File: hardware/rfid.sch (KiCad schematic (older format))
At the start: 1 part

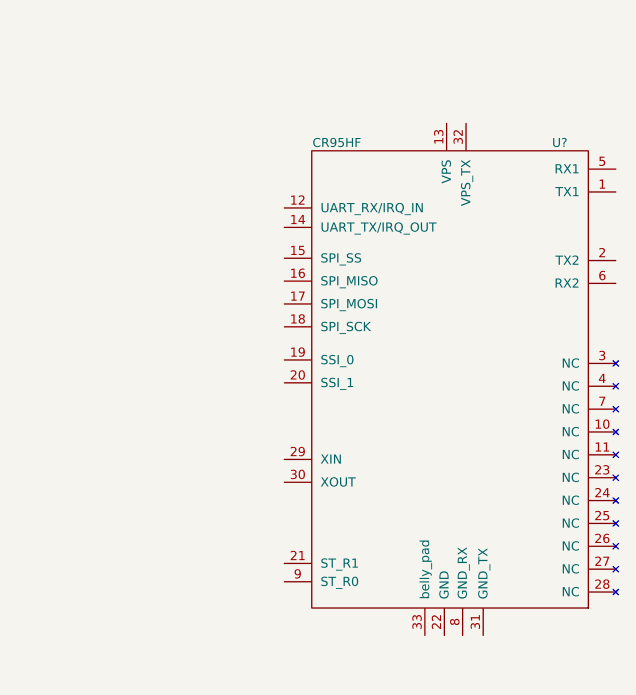
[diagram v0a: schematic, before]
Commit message: Added crystal and started connecting power to chip and extra pins.
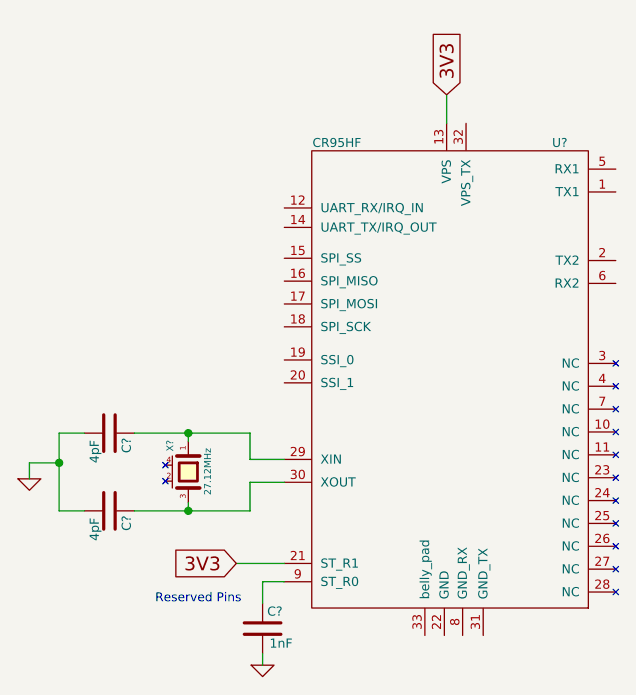
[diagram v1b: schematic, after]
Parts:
- added C? (x2): 4pF, symbol capacitor
- added C?: 1nF, symbol capacitor
- added X?: 27.12MHz, symbol MURATA_CRYSTAL_SMD
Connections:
- net 3V3: now reaches U?.13 (VPS)
- net 3V3: now also U?.21 (ST_R1)
- net at U?.29 (XIN): now also C?.1, X?.1
- net at U?.30 (XOUT): now also C?.1, X?.3
- net at U?.9 (ST_R0): now also C?.1
- new net GND: C?.2, C?.2, C?.2
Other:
- note added: "Reserved Pins"
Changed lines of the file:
@@
 	1    0    0    -1
 $EndComp
+$Comp
+L MURATA_CRYSTAL_SMD X?
+U 1 1 54173929
+P 2365 2700
+F 0 "X?" H 2250 2620 30  0000 C CNN
+F 1 "27.12MHz" H 2260 2785 30  0000 L CNN
+F 2 "" H 2365 2700 60  0000 C CNN
+F 3 "" H 2365 2700 60  0000 C CNN
+	1    2365 2700
+	0    1    1    0
+$EndComp
+$Comp
+L capacitor C?
+U 1 1 54173C81
+P 2020 2530
+F 0 "C?" H 2040 2605 40  0000 L CNN
+F 1 "4pF" H 2050 2465 40  0000 L CNN
+F 2 "" H 2058 2380 30  0000 C CNN
+F 3 "" H 2020 2530 60  0000 C CNN
+	1    2020 2530
+	0    1    1    0
+$EndComp
+$Comp
+L capacitor C?
+U 1 1 54173DFA
+P 2020 2870
+F 0 "C?" H 2040 2945 40  0000 L CNN
+F 1 "4pF" H 2050 2805 40  0000 L CNN
+F 2 "" H 2058 2720 30  0000 C CNN
+F 3 "" H 2020 2870 60  0000 C CNN
+	1    2020 2870
+	0    1    1    0
+$EndComp
+Wire Wire Line
+	2130 2530 2635 2530
+Wire Wire Line
+	2365 2530 2365 2565
+Wire Wire Line
+	2635 2530 2635 2645
+Wire Wire Line
+	2635 2645 2785 2645
+Connection ~ 2365 2530
+Wire Wire Line
+	2130 2870 2635 2870
+Wire Wire Line
+	2365 2870 2365 2835
+Wire Wire Line
+	2635 2870 2635 2745
+Wire Wire Line
+	2635 2745 2785 2745
+Connection ~ 2365 2870
+$Comp
+L GND #PWR?
+U 1 1 54173FD6
+P 1670 2730
+F 0 "#PWR?" H 1670 2730 30  0001 C CNN
+F 1 "GND" H 1670 2660 30  0001 C CNN
+F 2 "" H 1670 2730 60  0000 C CNN
+F 3 "" H 1670 2730 60  0000 C CNN
+	1    1670 2730
+	1    0    0    -1
+$EndComp
+Wire Wire Line
+	1910 2530 1800 2530
+Wire Wire Line
+	1800 2530 1800 2870
+Wire Wire Line
+	1800 2870 1910 2870
+Wire Wire Line
+	1800 2660 1670 2660
+Wire Wire Line
+	1670 2660 1670 2730
+Connection ~ 1800 2660
+$Comp
+L capacitor C?
+U 1 1 54175E86
+P 2690 3385
+F 0 "C?" H 2710 3460 40  0000 L CNN
+F 1 "1nF" H 2720 3320 40  0000 L CNN
+F 2 "" H 2728 3235 30  0000 C CNN
+F 3 "" H 2690 3385 60  0000 C CNN
+	1    2690 3385
+	1    0    0    -1
+$EndComp
+Wire Wire Line
+	2785 3180 2690 3180
+Wire Wire Line
+	2690 3180 2690 3275
+$Comp
+L GND #PWR?
+U 1 1 54175FA9
+P 2690 3545
+F 0 "#PWR?" H 2690 3545 30  0001 C CNN
+F 1 "GND" H 2690 3475 30  0001 C CNN
+F 2 "" H 2690 3545 60  0000 C CNN
+F 3 "" H 2690 3545 60  0000 C CNN
+	1    2690 3545
+	1    0    0    -1
+$EndComp
+Wire Wire Line
+	2690 3495 2690 3545
+Text Notes 2220 3280 0    39   ~ 0
+Reserved Pins
+Text GLabel 3495 1050 1    60   Input ~ 0
+3V3
+Wire Wire Line
+	3495 1175 3495 1050
+Text GLabel 2575 3100 0    60   Input ~ 0
+3V3
+Wire Wire Line
+	2785 3100 2575 3100
 $EndSCHEMATC

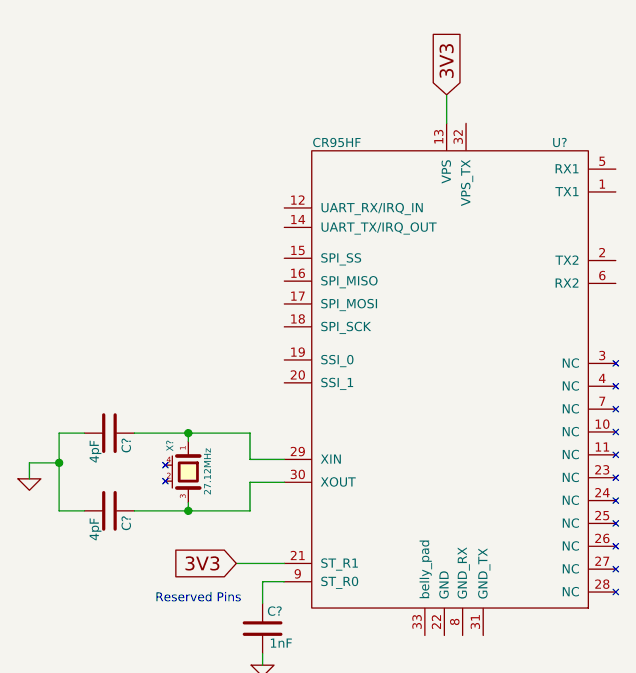
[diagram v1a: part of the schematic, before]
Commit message: Finished doing suggested pull ups, grounding, etc of certain pins. Added six pin connector for comms to micro. Not yet connected.
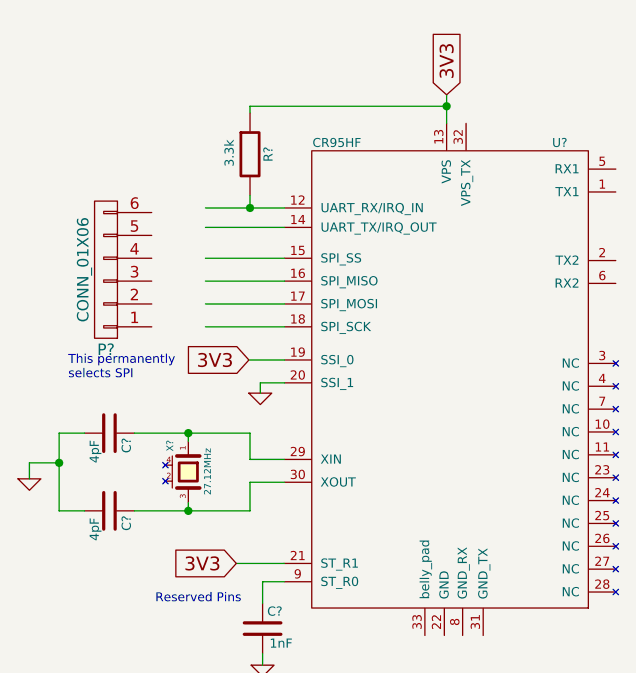
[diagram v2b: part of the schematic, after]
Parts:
- added P?: CONN_01X06, symbol CONN_01X06
- added R?: 3.3k, symbol resistor
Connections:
- wire segments 18 -> 35
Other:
- note added: "This permanently \nselects SPI"
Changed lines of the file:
@@
 $EndComp
 Wire Wire Line
-	2130 2530 2635 2530
+	2130 2530 2365 2530
+Wire Wire Line
+	2365 2530 2635 2530
 Wire Wire Line
 	2365 2530 2365 2565
@@
 Connection ~ 2365 2530
 Wire Wire Line
-	2130 2870 2635 2870
+	2130 2870 2365 2870
+Wire Wire Line
+	2365 2870 2635 2870
 Wire Wire Line
 	2365 2870 2365 2835
@@
 	1910 2530 1800 2530
 Wire Wire Line
-	1800 2530 1800 2870
+	1800 2530 1800 2660
+Wire Wire Line
+	1800 2660 1800 2870
 Wire Wire Line
 	1800 2870 1910 2870
@@
 3V3
 Wire Wire Line
-	3495 1175 3495 1050
+	3495 1175 3495 1100
+Wire Wire Line
+	3495 1100 3495 1050
 Text GLabel 2575 3100 0    60   Input ~ 0
 3V3
 Wire Wire Line
 	2785 3100 2575 3100
+$Comp
+L resistor R?
+U 1 1 54191892
+P 2635 1310
+F 0 "R?" V 2715 1310 40  0000 C CNN
+F 1 "3.3k" V 2545 1315 40  0000 C CNN
+F 2 "" V 2565 1310 30  0000 C CNN
+F 3 "" H 2635 1310 30  0000 C CNN
+	1    2635 1310
+	1    0    0    -1
+$EndComp
+Wire Wire Line
+	2440 1545 2635 1545
+Wire Wire Line
+	2635 1545 2785 1545
+Wire Wire Line
+	2635 1490 2635 1545
+Connection ~ 2635 1545
+Wire Wire Line
+	2635 1130 2635 1100
+Wire Wire Line
+	2635 1100 3495 1100
+Connection ~ 3495 1100
+$Comp
+L GND #PWR?
+U 1 1 54191BE5
+P 2680 2355
+F 0 "#PWR?" H 2680 2355 30  0001 C CNN
+F 1 "GND" H 2680 2285 30  0001 C CNN
+F 2 "" H 2680 2355 60  0000 C CNN
+F 3 "" H 2680 2355 60  0000 C CNN
+	1    2680 2355
+	1    0    0    -1
+$EndComp
+Text GLabel 2630 2210 0    60   Input ~ 0
+3V3
+Wire Wire Line
+	2785 2210 2630 2210
+Wire Wire Line
+	2785 2310 2680 2310
+Wire Wire Line
+	2680 2310 2680 2355
+Text Notes 1840 2300 0    39   ~ 0
+This permanently \nselects SPI
+Wire Wire Line
+	2785 1630 2440 1630
+Wire Wire Line
+	2785 1765 2440 1765
+Wire Wire Line
+	2785 1865 2440 1865
+Wire Wire Line
+	2785 1965 2440 1965
+Wire Wire Line
+	2785 2065 2440 2065
+$Comp
+L CONN_01X06 P?
+U 1 1 54192185
+P 2005 1815
+F 0 "P?" H 2005 2165 50  0000 C CNN
+F 1 "CONN_01X06" V 2105 1815 50  0000 C CNN
+F 2 "" H 2005 1815 60  0000 C CNN
+F 3 "" H 2005 1815 60  0000 C CNN
+	1    2005 1815
+	-1   0    0    1
+$EndComp
 $EndSCHEMATC

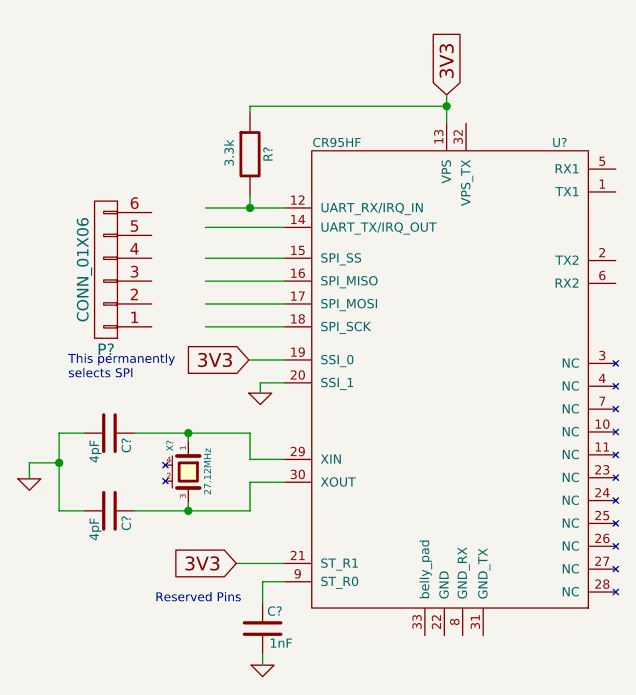
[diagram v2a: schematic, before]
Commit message: Added a few extra 3.3k resistors from 3V3 to pins just in case. They are in the demo board so I am guessing I should include them.
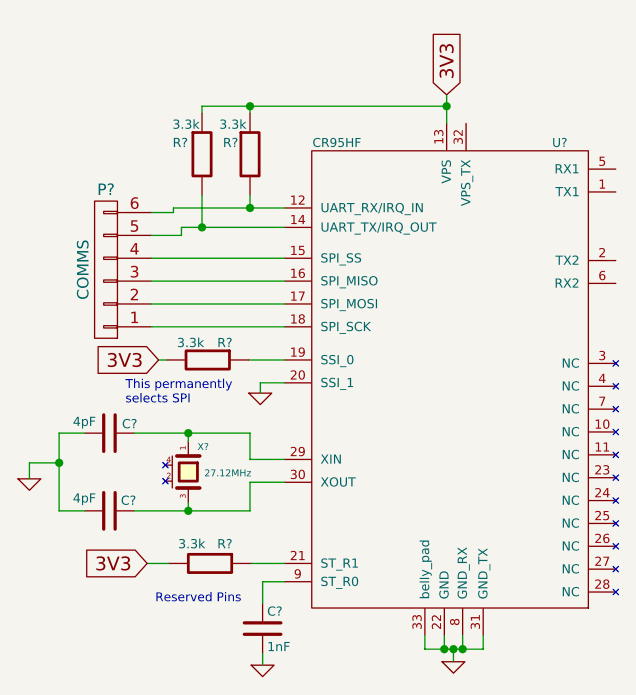
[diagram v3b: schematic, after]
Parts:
- added R? (x3): 3.3k, symbol resistor
- P?: value CONN_01X06 -> COMMS
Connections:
- wire segments 35 -> 44
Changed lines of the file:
@@
 U 1 1 54173929
 P 2365 2700
-F 0 "X?" H 2250 2620 30  0000 C CNN
-F 1 "27.12MHz" H 2260 2785 30  0000 L CNN
+F 0 "X?" V 2255 2765 30  0000 C CNN
+F 1 "27.12MHz" V 2370 2770 30  0000 L CNN
 F 2 "" H 2365 2700 60  0000 C CNN
 F 3 "" H 2365 2700 60  0000 C CNN
@@
 U 1 1 54173C81
 P 2020 2530
-F 0 "C?" H 2040 2605 40  0000 L CNN
-F 1 "4pF" H 2050 2465 40  0000 L CNN
+F 0 "C?" V 1980 2585 40  0000 L CNN
+F 1 "4pF" V 1970 2370 40  0000 L CNN
 F 2 "" H 2058 2380 30  0000 C CNN
 F 3 "" H 2020 2530 60  0000 C CNN
@@
 U 1 1 54173DFA
 P 2020 2870
-F 0 "C?" H 2040 2945 40  0000 L CNN
-F 1 "4pF" H 2050 2805 40  0000 L CNN
+F 0 "C?" V 1975 2920 40  0000 L CNN
+F 1 "4pF" V 1965 2710 40  0000 L CNN
 F 2 "" H 2058 2720 30  0000 C CNN
 F 3 "" H 2020 2870 60  0000 C CNN
@@
 $EndComp
 Wire Wire Line
-	2130 2530 2365 2530
-Wire Wire Line
-	2365 2530 2635 2530
+	2130 2530 2635 2530
 Wire Wire Line
 	2365 2530 2365 2565
@@
 Connection ~ 2365 2530
 Wire Wire Line
-	2130 2870 2365 2870
-Wire Wire Line
-	2365 2870 2635 2870
+	2130 2870 2635 2870
 Wire Wire Line
 	2365 2870 2365 2835
@@
 	1910 2530 1800 2530
 Wire Wire Line
-	1800 2530 1800 2660
-Wire Wire Line
-	1800 2660 1800 2870
+	1800 2530 1800 2870
 Wire Wire Line
 	1800 2870 1910 2870
@@
 P 2690 3385
 F 0 "C?" H 2710 3460 40  0000 L CNN
-F 1 "1nF" H 2720 3320 40  0000 L CNN
+F 1 "1nF" H 2710 3305 40  0000 L CNN
 F 2 "" H 2728 3235 30  0000 C CNN
 F 3 "" H 2690 3385 60  0000 C CNN
@@
 3V3
 Wire Wire Line
-	3495 1175 3495 1100
-Wire Wire Line
-	3495 1100 3495 1050
-Text GLabel 2575 3100 0    60   Input ~ 0
+	3495 1050 3495 1175
+Text GLabel 2185 3100 0    60   Input ~ 0
 3V3
-Wire Wire Line
-	2785 3100 2575 3100
 $Comp
 L resistor R?
 U 1 1 54191892
 P 2635 1310
-F 0 "R?" V 2715 1310 40  0000 C CNN
-F 1 "3.3k" V 2545 1315 40  0000 C CNN
+F 0 "R?" H 2550 1360 40  0000 C CNN
+F 1 "3.3k" H 2560 1440 40  0000 C CNN
 F 2 "" V 2565 1310 30  0000 C CNN
 F 3 "" H 2635 1310 30  0000 C CNN
@@
 $EndComp
 Wire Wire Line
-	2440 1545 2635 1545
-Wire Wire Line
-	2635 1545 2785 1545
+	2300 1545 2785 1545
 Wire Wire Line
 	2635 1490 2635 1545
@@
 	2635 1130 2635 1100
 Wire Wire Line
-	2635 1100 3495 1100
+	2425 1100 3495 1100
 Connection ~ 3495 1100
 $Comp
@@
 	1    0    0    -1
 $EndComp
-Text GLabel 2630 2210 0    60   Input ~ 0
+Text GLabel 2235 2210 0    60   Input ~ 0
 3V3
 Wire Wire Line
@@
 Wire Wire Line
 	2680 2310 2680 2355
-Text Notes 1840 2300 0    39   ~ 0
+Text Notes 2090 2410 0    39   ~ 0
 This permanently \nselects SPI
 Wire Wire Line
-	2785 1630 2440 1630
-Wire Wire Line
-	2785 1765 2440 1765
-Wire Wire Line
-	2785 1865 2440 1865
-Wire Wire Line
-	2785 1965 2440 1965
-Wire Wire Line
-	2785 2065 2440 2065
+	2335 1630 2785 1630
+Wire Wire Line
+	2205 1765 2785 1765
+Wire Wire Line
+	2205 1865 2785 1865
+Wire Wire Line
+	2205 1965 2785 1965
+Wire Wire Line
+	2205 2065 2785 2065
 $Comp
 L CONN_01X06 P?
 U 1 1 54192185
 P 2005 1815
-F 0 "P?" H 2005 2165 50  0000 C CNN
-F 1 "CONN_01X06" V 2105 1815 50  0000 C CNN
+F 0 "P?" H 2005 1465 50  0000 C CNN
+F 1 "COMMS" V 2105 1815 50  0000 C CNN
 F 2 "" H 2005 1815 60  0000 C CNN
 F 3 "" H 2005 1815 60  0000 C CNN
@@
 	-1   0    0    1
 $EndComp
+Wire Wire Line
+	2335 1630 2335 1665
+Wire Wire Line
+	2335 1665 2205 1665
+Wire Wire Line
+	2300 1545 2300 1565
+Wire Wire Line
+	2300 1565 2205 1565
+$Comp
+L resistor R?
+U 1 1 541A2E55
+P 2425 1310
+F 0 "R?" H 2330 1360 40  0000 C CNN
+F 1 "3.3k" H 2355 1440 40  0000 C CNN
+F 2 "" V 2355 1310 30  0000 C CNN
+F 3 "" H 2425 1310 30  0000 C CNN
+	1    2425 1310
+	1    0    0    -1
+$EndComp
+Wire Wire Line
+	2425 1490 2425 1630
+Connection ~ 2425 1630
+Wire Wire Line
+	2425 1130 2425 1100
+Connection ~ 2635 1100
+$Comp
+L resistor R?
+U 1 1 541A325E
+P 2450 2210
+F 0 "R?" V 2375 2285 40  0000 C CNN
+F 1 "3.3k" V 2375 2135 40  0000 C CNN
+F 2 "" V 2380 2210 30  0000 C CNN
+F 3 "" H 2450 2210 30  0000 C CNN
+	1    2450 2210
+	0    1    1    0
+$EndComp
+Wire Wire Line
+	2235 2210 2270 2210
+$Comp
+L resistor R?
+U 1 1 541A35D8
+P 2460 3100
+F 0 "R?" V 2375 3165 40  0000 C CNN
+F 1 "3.3k" V 2375 3020 40  0000 C CNN
+F 2 "" V 2390 3100 30  0000 C CNN
+F 3 "" H 2460 3100 30  0000 C CNN
+	1    2460 3100
+	0    1    1    0
+$EndComp
+Wire Wire Line
+	2785 3100 2640 3100
+Wire Wire Line
+	2185 3100 2280 3100
+$Comp
+L GND #PWR?
+U 1 1 541A40A6
+P 3525 3530
+F 0 "#PWR?" H 3525 3530 30  0001 C CNN
+F 1 "GND" H 3525 3460 30  0001 C CNN
+F 2 "" H 3525 3530 60  0000 C CNN
+F 3 "" H 3525 3530 60  0000 C CNN
+	1    3525 3530
+	1    0    0    -1
+$EndComp
+Wire Wire Line
+	3655 3415 3655 3475
+Wire Wire Line
+	3655 3475 3400 3475
+Wire Wire Line
+	3400 3475 3400 3415
+Wire Wire Line
+	3485 3415 3485 3475
+Connection ~ 3485 3475
+Wire Wire Line
+	3565 3415 3565 3475
+Connection ~ 3565 3475
+Wire Wire Line
+	3525 3475 3525 3530
+Connection ~ 3525 3475
 $EndSCHEMATC
